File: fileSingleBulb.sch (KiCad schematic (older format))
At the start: 4 parts

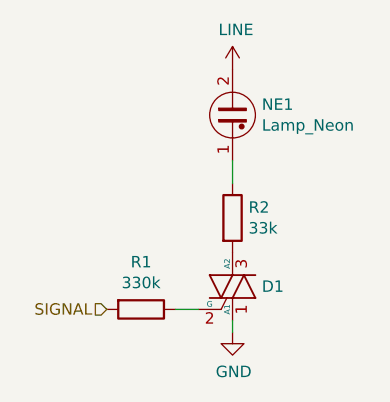
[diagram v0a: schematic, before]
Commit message: Add isolation
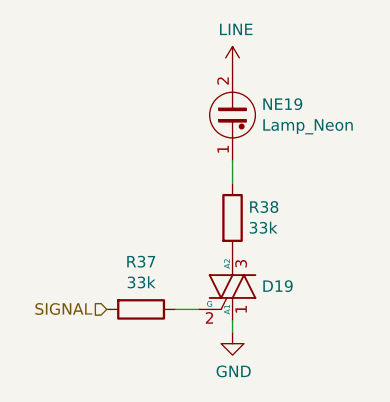
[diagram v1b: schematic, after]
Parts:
- R1: value 330k -> 33k; LCSC C25778 -> C25779
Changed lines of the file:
@@
 $Descr A4 11693 8268
 encoding utf-8
-Sheet 3 73
+Sheet 23 73
 Title ""
 Date ""
@@
 AR Path="/5EFAAFE1/5EF2B9F7/5EF0ED9C" Ref="R111"  Part="1"
 AR Path="/5EFAAFEB/5EF2B9F7/5EF0ED9C" Ref="R127"  Part="1"
-F 0 "R1" V 843 1850 50  0000 C CNN
-F 1 "330k" V 934 1850 50  0000 C CNN
+F 0 "R37" V 843 1850 50  0000 C CNN
+F 1 "33k" V 934 1850 50  0000 C CNN
 F 2 "Resistor_SMD:R_0402_1005Metric" V 980 1850 50  0001 C CNN
 F 3 "~" H 1050 1850 50  0001 C CNN
-F 4 "C25778" V 1050 1850 50  0001 C CNN "LCSC"
+F 4 "C25779" V 1050 1850 50  0001 C CNN "LCSC"
 	1    1050 1850
 	0    1    1    0
@@
 AR Path="/5EFAAFE1/5EF2B9F7/5EF0EDA3" Ref="R112"  Part="1"
 AR Path="/5EFAAFEB/5EF2B9F7/5EF0EDA3" Ref="R128"  Part="1"
-F 0 "R2" H 1520 1496 50  0000 L CNN
+F 0 "R38" H 1520 1496 50  0000 L CNN
 F 1 "33k" H 1520 1405 50  0000 L CNN
 F 2 "Resistor_SMD:R_0603_1608Metric" V 1380 1450 50  0001 C CNN
@@
 AR Path="/5EFAAFE1/5EF2B9F7/5EF0EDA9" Ref="#PWR0246"  Part="1"
 AR Path="/5EFAAFEB/5EF2B9F7/5EF0EDA9" Ref="#PWR0267"  Part="1"
-F 0 "#PWR0106" H 1450 650 50  0001 C CNN
+F 0 "#PWR0152" H 1450 650 50  0001 C CNN
 F 1 "LINE" H 1465 973 50  0000 C CNN
 F 2 "" H 1450 800 50  0001 C CNN
@@
 AR Path="/5EFAAFE1/5EF2B9F7/5EF0EDB1" Ref="#PWR0247"  Part="1"
 AR Path="/5EFAAFEB/5EF2B9F7/5EF0EDB1" Ref="#PWR0268"  Part="1"
-F 0 "#PWR0107" H 1450 1700 50  0001 C CNN
+F 0 "#PWR0153" H 1450 1700 50  0001 C CNN
 F 1 "GND" H 1455 1777 50  0000 C CNN
 F 2 "" H 1450 1950 50  0001 C CNN
@@
 AR Path="/5EFAAFE1/5EF2B9F7/5EF0EDBE" Ref="D56"  Part="1"
 AR Path="/5EFAAFEB/5EF2B9F7/5EF0EDBE" Ref="D64"  Part="1"
-F 0 "D1" H 1578 1750 50  0000 L CNN
+F 0 "D19" H 1578 1750 50  0000 L CNN
 F 1 "Q_TRIAC_A1GA2" H 1578 1705 50  0001 L CNN
 F 2 "Package_TO_SOT_SMD:SOT-23" V 1525 1775 50  0001 C CNN
@@
 AR Path="/5EFAAFE1/5EF2B9F7/5EF0EDB7" Ref="NE56"  Part="1"
 AR Path="/5EFAAFEB/5EF2B9F7/5EF0EDB7" Ref="NE64"  Part="1"
-F 0 "NE1" H 1578 1046 50  0000 L CNN
+F 0 "NE19" H 1578 1046 50  0000 L CNN
 F 1 "Lamp_Neon" H 1578 955 50  0000 L CNN
 F 2 "NeonMatrix_Connector:NeonBulb" V 1450 1100 50  0001 C CNN

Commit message: Add routing
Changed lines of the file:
@@
 AR Path="/5EFAAFE1/5EF2B9F7/5EF0ED9C" Ref="R111"  Part="1"
 AR Path="/5EFAAFEB/5EF2B9F7/5EF0ED9C" Ref="R127"  Part="1"
-F 0 "R37" V 843 1850 50  0000 C CNN
+F 0 "R127" V 843 1850 50  0000 C CNN
 F 1 "33k" V 934 1850 50  0000 C CNN
 F 2 "Resistor_SMD:R_0402_1005Metric" V 980 1850 50  0001 C CNN
@@
 AR Path="/5EFAAFE1/5EF2B9F7/5EF0EDA3" Ref="R112"  Part="1"
 AR Path="/5EFAAFEB/5EF2B9F7/5EF0EDA3" Ref="R128"  Part="1"
-F 0 "R38" H 1520 1496 50  0000 L CNN
+F 0 "R128" H 1520 1496 50  0000 L CNN
 F 1 "33k" H 1520 1405 50  0000 L CNN
 F 2 "Resistor_SMD:R_0603_1608Metric" V 1380 1450 50  0001 C CNN
@@
 AR Path="/5EFAAFE1/5EF2B9F7/5EF0EDA9" Ref="#PWR0246"  Part="1"
 AR Path="/5EFAAFEB/5EF2B9F7/5EF0EDA9" Ref="#PWR0267"  Part="1"
-F 0 "#PWR0152" H 1450 650 50  0001 C CNN
+F 0 "#PWR0267" H 1450 650 50  0001 C CNN
 F 1 "LINE" H 1465 973 50  0000 C CNN
 F 2 "" H 1450 800 50  0001 C CNN
@@
 AR Path="/5EFAAFE1/5EF2B9F7/5EF0EDB1" Ref="#PWR0247"  Part="1"
 AR Path="/5EFAAFEB/5EF2B9F7/5EF0EDB1" Ref="#PWR0268"  Part="1"
-F 0 "#PWR0153" H 1450 1700 50  0001 C CNN
+F 0 "#PWR0268" H 1450 1700 50  0001 C CNN
 F 1 "GND" H 1455 1777 50  0000 C CNN
 F 2 "" H 1450 1950 50  0001 C CNN
@@
 AR Path="/5EFAAFE1/5EF2B9F7/5EF0EDBE" Ref="D56"  Part="1"
 AR Path="/5EFAAFEB/5EF2B9F7/5EF0EDBE" Ref="D64"  Part="1"
-F 0 "D19" H 1578 1750 50  0000 L CNN
+F 0 "D64" H 1578 1750 50  0000 L CNN
 F 1 "Q_TRIAC_A1GA2" H 1578 1705 50  0001 L CNN
 F 2 "Package_TO_SOT_SMD:SOT-23" V 1525 1775 50  0001 C CNN
@@
 AR Path="/5EFAAFE1/5EF2B9F7/5EF0EDB7" Ref="NE56"  Part="1"
 AR Path="/5EFAAFEB/5EF2B9F7/5EF0EDB7" Ref="NE64"  Part="1"
-F 0 "NE19" H 1578 1046 50  0000 L CNN
+F 0 "NE64" H 1578 1046 50  0000 L CNN
 F 1 "Lamp_Neon" H 1578 955 50  0000 L CNN
 F 2 "NeonMatrix_Connector:NeonBulb" V 1450 1100 50  0001 C CNN

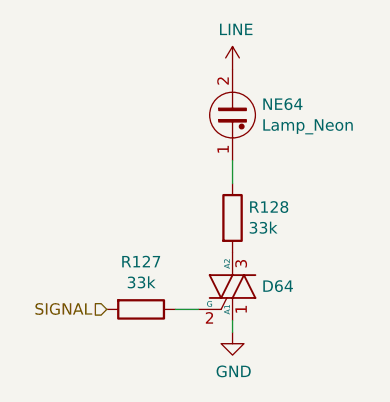
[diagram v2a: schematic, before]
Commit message: Add bulk capacitance, fix isolation, silkscreen and vias
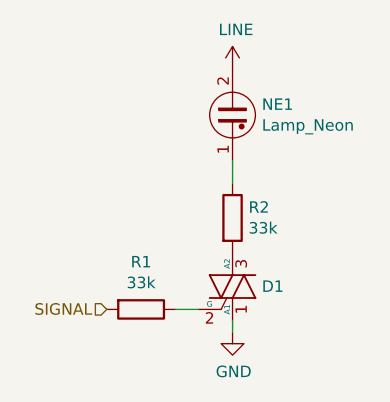
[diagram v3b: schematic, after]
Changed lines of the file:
@@
 $Descr A4 11693 8268
 encoding utf-8
-Sheet 23 73
+Sheet 3 73
 Title ""
 Date ""
@@
 AR Path="/5EFAAFE1/5EF2B9F7/5EF0ED9C" Ref="R111"  Part="1"
 AR Path="/5EFAAFEB/5EF2B9F7/5EF0ED9C" Ref="R127"  Part="1"
-F 0 "R127" V 843 1850 50  0000 C CNN
+F 0 "R1" V 843 1850 50  0000 C CNN
 F 1 "33k" V 934 1850 50  0000 C CNN
 F 2 "Resistor_SMD:R_0402_1005Metric" V 980 1850 50  0001 C CNN
@@
 AR Path="/5EFAAFE1/5EF2B9F7/5EF0EDA3" Ref="R112"  Part="1"
 AR Path="/5EFAAFEB/5EF2B9F7/5EF0EDA3" Ref="R128"  Part="1"
-F 0 "R128" H 1520 1496 50  0000 L CNN
+F 0 "R2" H 1520 1496 50  0000 L CNN
 F 1 "33k" H 1520 1405 50  0000 L CNN
 F 2 "Resistor_SMD:R_0603_1608Metric" V 1380 1450 50  0001 C CNN
@@
 AR Path="/5EFAAFE1/5EF2B9F7/5EF0EDA9" Ref="#PWR0246"  Part="1"
 AR Path="/5EFAAFEB/5EF2B9F7/5EF0EDA9" Ref="#PWR0267"  Part="1"
-F 0 "#PWR0267" H 1450 650 50  0001 C CNN
+F 0 "#PWR0106" H 1450 650 50  0001 C CNN
 F 1 "LINE" H 1465 973 50  0000 C CNN
 F 2 "" H 1450 800 50  0001 C CNN
@@
 AR Path="/5EFAAFE1/5EF2B9F7/5EF0EDB1" Ref="#PWR0247"  Part="1"
 AR Path="/5EFAAFEB/5EF2B9F7/5EF0EDB1" Ref="#PWR0268"  Part="1"
-F 0 "#PWR0268" H 1450 1700 50  0001 C CNN
+F 0 "#PWR0107" H 1450 1700 50  0001 C CNN
 F 1 "GND" H 1455 1777 50  0000 C CNN
 F 2 "" H 1450 1950 50  0001 C CNN
@@
 AR Path="/5EFAAFE1/5EF2B9F7/5EF0EDBE" Ref="D56"  Part="1"
 AR Path="/5EFAAFEB/5EF2B9F7/5EF0EDBE" Ref="D64"  Part="1"
-F 0 "D64" H 1578 1750 50  0000 L CNN
+F 0 "D1" H 1578 1750 50  0000 L CNN
 F 1 "Q_TRIAC_A1GA2" H 1578 1705 50  0001 L CNN
 F 2 "Package_TO_SOT_SMD:SOT-23" V 1525 1775 50  0001 C CNN
@@
 AR Path="/5EFAAFE1/5EF2B9F7/5EF0EDB7" Ref="NE56"  Part="1"
 AR Path="/5EFAAFEB/5EF2B9F7/5EF0EDB7" Ref="NE64"  Part="1"
-F 0 "NE64" H 1578 1046 50  0000 L CNN
+F 0 "NE1" H 1578 1046 50  0000 L CNN
 F 1 "Lamp_Neon" H 1578 955 50  0000 L CNN
 F 2 "NeonMatrix_Connector:NeonBulb" V 1450 1100 50  0001 C CNN

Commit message: RevA, Add production files
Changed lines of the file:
@@
 AR Path="/5EFAAFE1/5EF2B9F7/5EF0ED9C" Ref="R111"  Part="1"
 AR Path="/5EFAAFEB/5EF2B9F7/5EF0ED9C" Ref="R127"  Part="1"
-F 0 "R1" V 843 1850 50  0000 C CNN
+F 0 "R127" V 843 1850 50  0000 C CNN
 F 1 "33k" V 934 1850 50  0000 C CNN
 F 2 "Resistor_SMD:R_0402_1005Metric" V 980 1850 50  0001 C CNN
@@
 AR Path="/5EFAAFE1/5EF2B9F7/5EF0EDA3" Ref="R112"  Part="1"
 AR Path="/5EFAAFEB/5EF2B9F7/5EF0EDA3" Ref="R128"  Part="1"
-F 0 "R2" H 1520 1496 50  0000 L CNN
+F 0 "R128" H 1520 1496 50  0000 L CNN
 F 1 "33k" H 1520 1405 50  0000 L CNN
 F 2 "Resistor_SMD:R_0603_1608Metric" V 1380 1450 50  0001 C CNN
@@
 AR Path="/5EFAAFE1/5EF2B9F7/5EF0EDA9" Ref="#PWR0246"  Part="1"
 AR Path="/5EFAAFEB/5EF2B9F7/5EF0EDA9" Ref="#PWR0267"  Part="1"
-F 0 "#PWR0106" H 1450 650 50  0001 C CNN
+F 0 "#PWR0267" H 1450 650 50  0001 C CNN
 F 1 "LINE" H 1465 973 50  0000 C CNN
 F 2 "" H 1450 800 50  0001 C CNN
@@
 AR Path="/5EFAAFE1/5EF2B9F7/5EF0EDB1" Ref="#PWR0247"  Part="1"
 AR Path="/5EFAAFEB/5EF2B9F7/5EF0EDB1" Ref="#PWR0268"  Part="1"
-F 0 "#PWR0107" H 1450 1700 50  0001 C CNN
+F 0 "#PWR0268" H 1450 1700 50  0001 C CNN
 F 1 "GND" H 1455 1777 50  0000 C CNN
 F 2 "" H 1450 1950 50  0001 C CNN
@@
 AR Path="/5EFAAFE1/5EF2B9F7/5EF0EDBE" Ref="D56"  Part="1"
 AR Path="/5EFAAFEB/5EF2B9F7/5EF0EDBE" Ref="D64"  Part="1"
-F 0 "D1" H 1578 1750 50  0000 L CNN
+F 0 "D64" H 1578 1750 50  0000 L CNN
 F 1 "Q_TRIAC_A1GA2" H 1578 1705 50  0001 L CNN
 F 2 "Package_TO_SOT_SMD:SOT-23" V 1525 1775 50  0001 C CNN
@@
 AR Path="/5EFAAFE1/5EF2B9F7/5EF0EDB7" Ref="NE56"  Part="1"
 AR Path="/5EFAAFEB/5EF2B9F7/5EF0EDB7" Ref="NE64"  Part="1"
-F 0 "NE1" H 1578 1046 50  0000 L CNN
+F 0 "NE64" H 1578 1046 50  0000 L CNN
 F 1 "Lamp_Neon" H 1578 955 50  0000 L CNN
 F 2 "NeonMatrix_Connector:NeonBulb" V 1450 1100 50  0001 C CNN
